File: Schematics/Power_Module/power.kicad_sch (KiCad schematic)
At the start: 67 parts, among them J2 ScrewSwitch, J3 Battery, J6 ScrewSwitch, J7 Battery, Q1 AO4447A, Q2 AO4447A, U1 LMR51430YDDCR, U10 TPS61175PWPR, U2 LMR51430YDDCR, U3 ACS37041KLHBLT-010B3, U4 AMS1117-3.3, U5 ACS37041KLHBLT-010B3, U6 LM66100DCKR, U7 LM66100DCKR, U8 LM66100DCKR

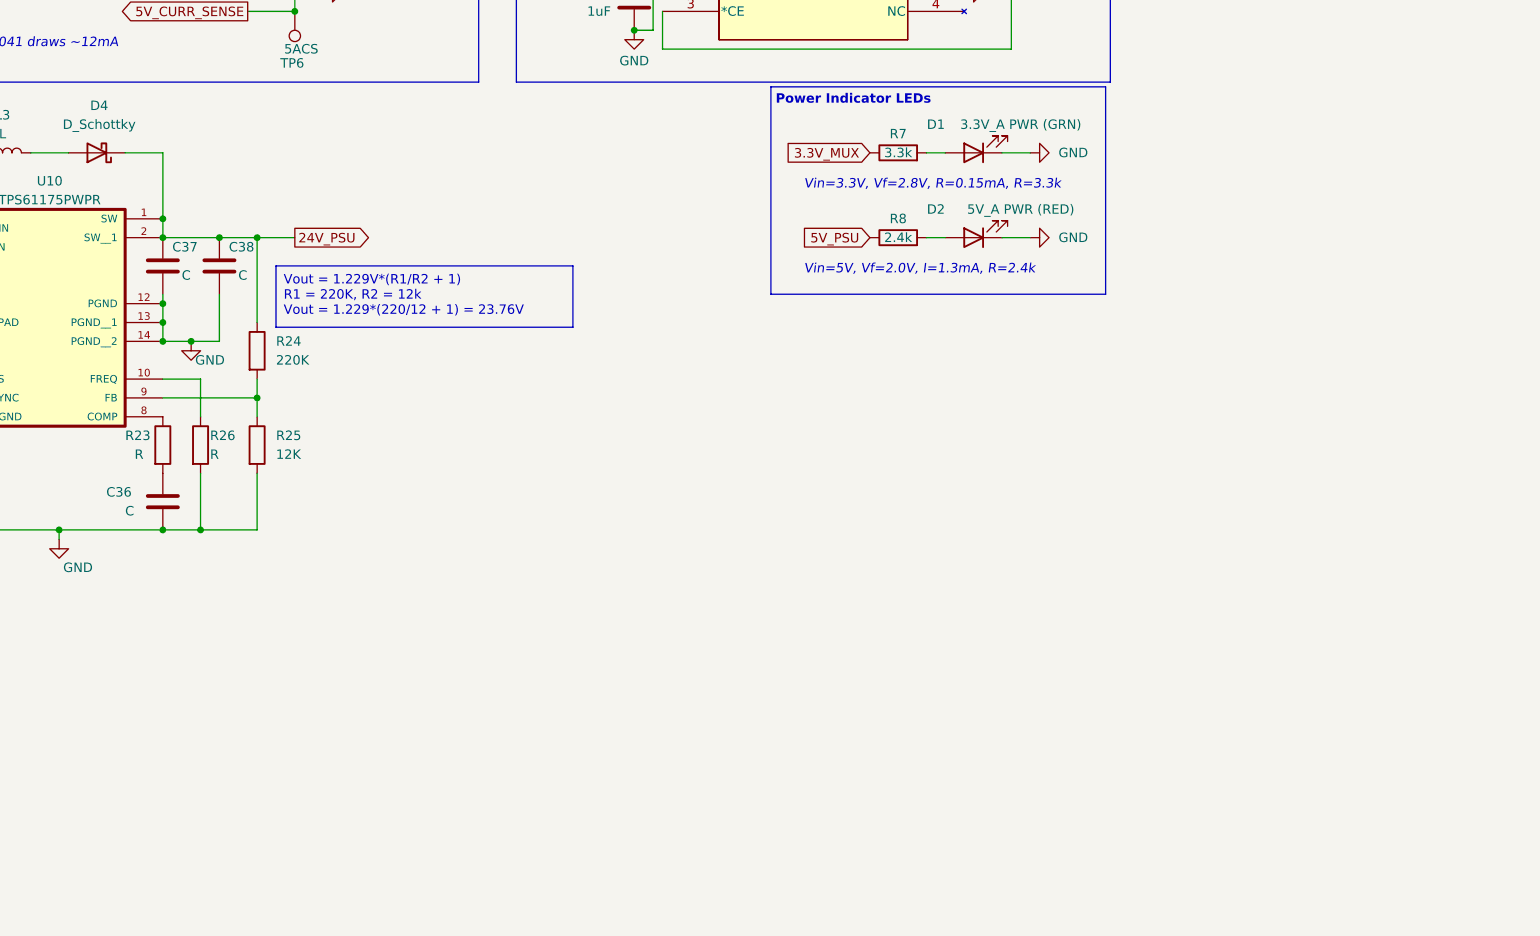
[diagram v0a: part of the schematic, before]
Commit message: cleaned up boost pdf & lcsc and noted next steps
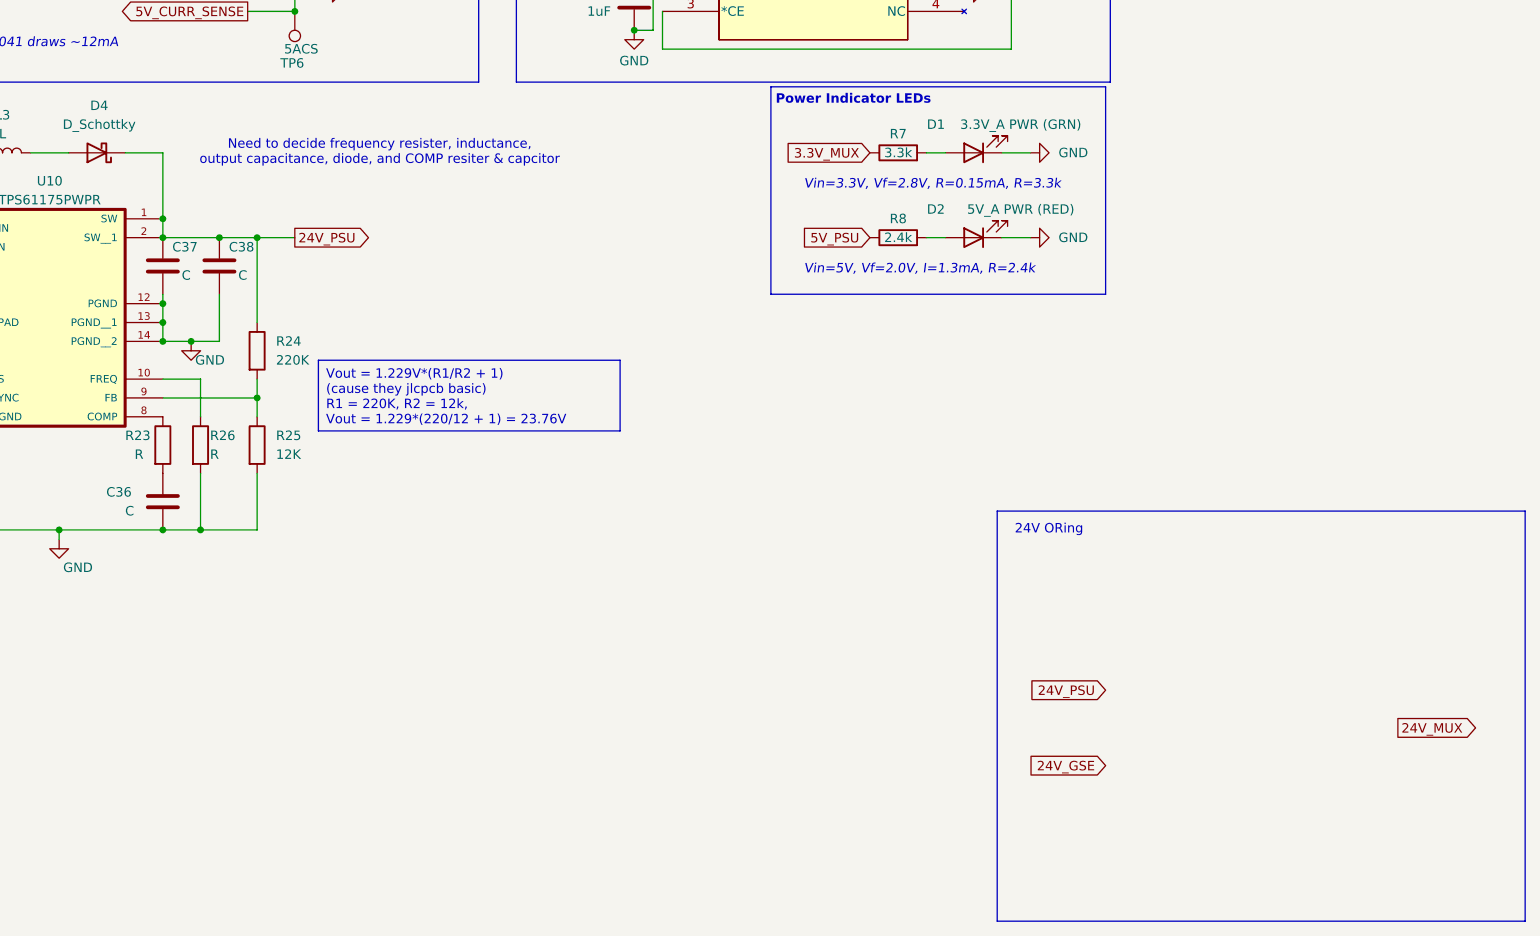
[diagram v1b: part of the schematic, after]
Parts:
- U10: LCSC (none) -> C43276
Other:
- note added: "24V ORing"
- note added: "Need to decide frequency resister, inductance, output capacitance, diode, and COMP resiter & capcitor"
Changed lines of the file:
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@@
+	)
+	(rectangle
+		(start 269.875 140.97)
+		(end 340.995 196.215)
+		(stroke
+			(width 0)
+			(type default)
+		)
+		(fill
+			(type none)
+		)
 	)
 	(rectangle
@@
 		)
 	)
-	(text_box "Vout = 1.229V*(R1/R2 + 1)\nR1 = 220K, R2 = 12k\nVout = 1.229*(220/12 + 1) = 23.76V"
-		(exclude_from_sim no)
-		(at 172.72 107.95 0)
-		(size 40.005 8.255)
+	(text_box "Vout = 1.229V*(R1/R2 + 1)\n(cause they jlcpcb basic)\nR1 = 220K, R2 = 12k, \nVout = 1.229*(220/12 + 1) = 23.76V"
+		(exclude_from_sim no)
+		(at 178.435 120.65 0)
+		(size 40.64 9.525)
 		(stroke
 			(width 0)
@@
 		)
 	)
+	(text "Need to decide frequency resister, inductance, \noutput capacitance, diode, and COMP resiter & capcitor"
+		(exclude_from_sim no)
+		(at 186.69 92.71 0)
+		(effects
+			(font
+				(size 1.27 1.27)
+			)
+		)
+	)
 	(text "3.3V USB Regulator"
 		(exclude_from_sim no)
@@
 			)
 			(justify left bottom)
+		)
+	)
+	(text "24V ORing"
+		(exclude_from_sim no)
+		(at 276.86 143.51 0)
+		(effects
+			(font
+				(size 1.27 1.27)
+			)
 		)
 	)
@@
 		)
 	)
+	(global_label "24V_MUX"
+		(shape output)
+		(at 323.85 170.18 0)
+		(fields_autoplaced yes)
+		(effects
+			(font
+				(size 1.27 1.27)
+			)
+			(justify left)
+		)
+		(property "Intersheetrefs" "${INTERSHEET_REFS}"
+			(at 335.3018 170.18 0)
+			(effects
+				(font
+					(size 1.27 1.27)
+				)
+				(justify left)
+				(hide yes)
+			)
+		)
+	)
 	(global_label "5V_PSU"
 		(shape output)
@@
 		)
 	)
+	(global_label "24V_PSU"
+		(shape input)
+		(at 284.48 165.1 180)
+		(fields_autoplaced yes)
+		(effects
+			(font
+				(size 1.27 1.27)
+			)
+			(justify right)
+		)
+		(property "Intersheetrefs" "${INTERSHEET_REFS}"
+			(at 273.2096 165.1 0)
+			(effects
+				(font
+					(size 1.27 1.27)
+				)
+				(justify right)
+				(hide yes)
+			)
+		)
+	)
 	(global_label "BATT"
 		(shape input)
@@
 		(property "Intersheetrefs" "${INTERSHEET_REFS}"
 			(at 99.401 102.87 0)
+			(effects
+				(font
+					(size 1.27 1.27)
+				)
+				(justify right)
+				(hide yes)
+			)
+		)
+	)
+	(global_label "24V_GSE"
+		(shape input)
+		(at 284.48 175.26 180)
+		(fields_autoplaced yes)
+		(effects
+			(font
+				(size 1.27 1.27)
+			)
+			(justify right)
+		)
+		(property "Intersheetrefs" "${INTERSHEET_REFS}"
+			(at 273.3911 175.26 0)
 			(effects
 				(font
@@
 			)
 		)
-		(property "Datasheet" ""
+		(property "Datasheet" "${KIPRJMOD}/../../Datasheets/tps61175.pdf"
 			(at 139.7 115.57 0)
 			(effects
@@
 			(at 139.7 115.57 0)
 			(effects
+				(font
+					(size 1.27 1.27)
+				)
+				(hide yes)
+			)
+		)
+		(property "LCSC" "C43276"
+			(at 139.7 115.57 0)
+			(effects

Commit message: adding power ORing circuit
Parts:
- added C39, C41, C42, C43: 1uF, Capacitor_SMD:C_0603_1608Metric, symbol Device:C
- added C40: 100uF, symbol Device:C_Polarized
- added Q3, Q4: AO3400A, Package_TO_SOT_SMD:SOT-23, symbol Transistor_FET:AO3400A
- added U14, U15: LM74700QDBVRQ1, Package_TO_SOT_SMD:SOT-23-6, symbol Power_Management:LM74700
- J7: value Battery -> GSE
- TP2: value GND1 -> BATT_GND1
- TP9: value GND1 -> GSE_GND1
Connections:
- net 24V_GSE: now also C39.1, C42.1, Q3.2 (S), U14.1 (VCAP), U14.3 (EN), U14.6 (ANODE)
- net 24V_MUX: now also C40.1, Q3.3 (D), Q4.3 (D), U14.4 (CATHODE), U15.4 (CATHODE)
- net 24V_PSU: now also C41.2, C43.2, Q4.2 (S), U15.1 (VCAP), U15.3 (EN), U15.6 (ANODE)
- net GND: now also C39.2, C40.2, C41.1, C42.2, C43.1, U14.2 (GND), U15.2 (GND)
- net BATT renamed V_BATT
- new net: Q4.1 (G), U15.5 (GATE)
- new net: Q3.1 (G), U14.5 (GATE)
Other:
- note added: "Battery side needs GND protection circuitry"
- note added: "Primary 24V Boost Regulator"
- moved on the sheet: C33, C34, C35, C36, C37, C38, D1, D2, D4, J2, J3, J6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

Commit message: add equations for Boost and instructions for buck design changes
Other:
- note added: "Switch 2 500000 Hz system!! (less switching loss) originally designed for component footprint Now design for increase efficient!!"
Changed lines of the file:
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@@
+		)
+	)
+	(text_box "Equations:\nD = 1 - Vin/Vo\nT = 1/F\nIin = Vin/(R(1-D)^2)\ndetla_IL = 30% of IL\nL = VinDT/L\nLcrit = RT/2(1-D)^2D (when IL = 0)\nIL_max = Iin + 1/2(delta_IL)\ndelta_Vc = VoDT/RC\nID_avg = Iin(1-D)\nId_max = IL_max\nVc_max = Vo\nIc_rms = sqrt(DIin^2 + (1-D)(Iin - Io) \n\n\nConstants:\nF = 200KHz to 2.2MHz (Choose lowest frequency feasable, smaller F -> large L and C)\nVin_max = 12.6V\nVin_nominal = 11.1V\nVin_min = 7.5V\nVo = 23.76V ~ 24V\nPo_max = 10W\nPo_min = 1W\nD_max = 1 - 7.5/24\nD_min = 1 - 12.6/24\n\n\n\n"
+		(exclude_from_sim no)
+		(at 251.8918 169.164 0)
+		(size 58.166 61.7982)
+		(stroke
+			(width 0)
+			(type default)
+		)
+		(fill
+			(type none)
+		)
+		(effects
+			(font
+				(size 1.27 1.27)
+			)
+			(justify left top)
 		)
 	)
@@
 		)
 	)
+	(text "Switch 2 500000 Hz system!! (less switching loss)\noriginally designed for component footprint\nNow design for increase efficient!!"
+		(exclude_from_sim no)
+		(at -48.26 2.54 0)
+		(effects
+			(font
+				(size 1.27 1.27)
+				(thickness 0.254)
+				(bold yes)
+			)
+		)
+	)

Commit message: Update power.kicad_sch
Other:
- note added: "Switched to a 500 000 Hz system for increase in efficiency."
- note removed: "Switch 2 500000 Hz system!! (less switching loss) originally designed for component footprint Now design for increase efficient!!"
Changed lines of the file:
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@@
 		)
 	)
-	(text_box "Constants:\nT = 1/1100000\nVin = 24V\nVout = 5\nD = 5/24\n\nP = 0.2W\nLcrit = 0.5(1-.2083)(5^2/0.2)*(1/1100000) = 45uH\n\nP=1W (typical with RF transmition)\nLcrit = 0.5(1-.2083)(5^2/1)*(1/1100000) = 9uH\ndelta IL = 0.3(1/5) = 0.06A\nL = 5(1-0.2083)(1/1100000)/(0.08) = 60uH\nILmax = (1/5) + 0.5*(0.06) = 0.23A\n\nChose Inductor 68uH, ILmax = 1A\ndelta_IL = 5(1-0.2083)/(1100000*68*10^-6) = 0.053A\ndelta_Vo = 2%*5 = 0.1V\nC = 0.053/(8*1100000*0.1) = 0.06uF"
+	(text_box "Constants:\nT = 1/500000\nVin = 24V\nVout = 5\nD = 5/24\n\nP = 0.2W\nLcrit = 0.5(1-0.2083)(5^2/0.2)*(1/500000) = 99uH\n\nP=1W (typical with RF transmition)\nLcrit = 0.5(1-0.2083)(5^2/1)*(1/500000) = 20uH\n\ndelta IL = 0.3(1/5) = 0.06A\nL = 5(1-0.2083)(1/500000)/(0.06) = 132uH\nILmax = (1/5) + 0.5*(0.06) = 0.23A\n\nChose Inductor 130uH, ILmax = 1A\ndelta_IL = 5(1-0.2083)/(500000*130*10^-6) = 0.061A\ndelta_Vo = 2%*5 = 0.1V\nC = 0.061/(8*500000*0.1) = 0.15uF"
 		(exclude_from_sim no)
 		(at -80.645 93.345 0)
@@
 		)
 	)
-	(text_box "Constants:\nT = 1/1100000\nVin = 24V\nVout = 3.3V\nD = 3.3/24 = 0.1375\n\nP = 0.5W (estimate with one module powered)\nLcrit = 0.5*(1-0.1375)*(3.3^2/0.5)*(1/1100000) = 2.6uH\n\nPo = 3W (estimate of all 3.3V modules)\nLcrit = 0.5*(1-0.1375)*(3.3^2/3)*(1/1100000) = 0.43uH\n\ndelta_IL = 0.3*(3/3.3) = 0.273A\nL = 3.3*(1-0.1375)/(1100000*0.273) = 9.5uH\nILmax = (3/3.3) + 0.5*0.273 = 1.05A\n\n\nChose 10uH Inductor, ILmax = 2.5\ndelta_IL = 3.3*(1-0.1375)/(1100000*10*10^-6) = 0.26A\ndelta_Vo = 2%*3.3 = 0.066V\nC = 0.26/(8*1100000*0.066) = 0.45uF"
-		(exclude_from_sim no)
-		(at -80.645 46.99 0)
-		(size 60.325 44.45)
+	(text_box "Constants:\nT = 1/500000\nVin = 24V\nVout = 3.3V\nD = 3.3/24 = 0.1375\n\nP = 0.5W (estimate with one module powered)\nLcrit = 0.5*(1-0.1375)*(3.3^2/0.5)*(1/500000) = 18.79uH\n\nPo = 3W (estimate of all 3.3V modules)\nLcrit = 0.5*(1-0.1375)*(3.3^2/3)*(1/500000) = 3.13uH\n\ndelta_IL = 0.3*(3/3.3) = 0.273A\nL = 3.3*(1-0.1375)/(500000*0.273) = 20.85uH\nILmax = (3/3.3) + 0.5*0.273 = 1.05A\n\n\nChose 22uH Inductor, ILmax = 2.2 \ndelta_IL = 3.3*(1-0.1375)/(500000*22*10^-6) = 0.26A\ndelta_Vo = 2%*3.3 = 0.066V\nC = 0.26/(8*500000*0.066) = 0.98uF"
+		(exclude_from_sim no)
+		(at -81.28 46.99 0)
+		(size 62.23 44.45)
 		(stroke
 			(width 0)
@@
 		)
 	)
-	(text "Switch 2 500000 Hz system!! (less switching loss)\noriginally designed for component footprint\nNow design for increase efficient!!"
+	(text "Switched to a 500 000 Hz system for increase in efficiency."
 		(exclude_from_sim no)
 		(at -48.26 2.54 0)

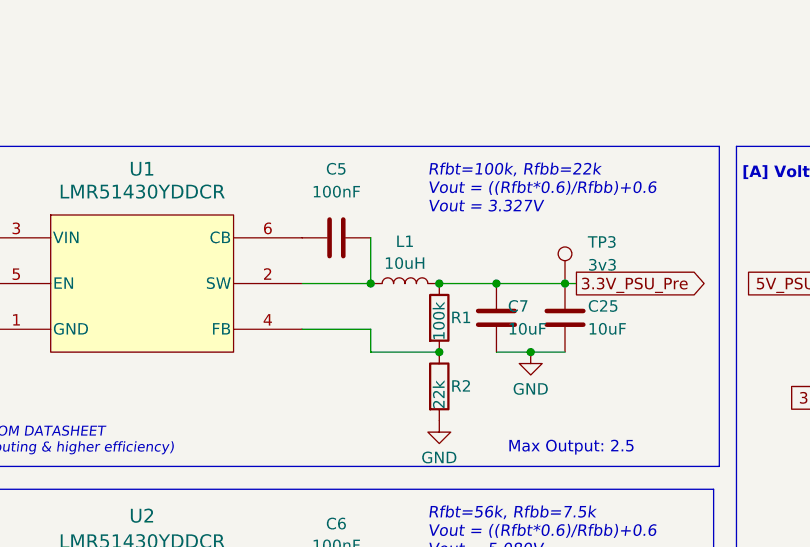
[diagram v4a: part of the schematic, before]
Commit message: Update power.kicad_sch
Changed frequency to 500 000Hz and updated schematics (not the new footprint)
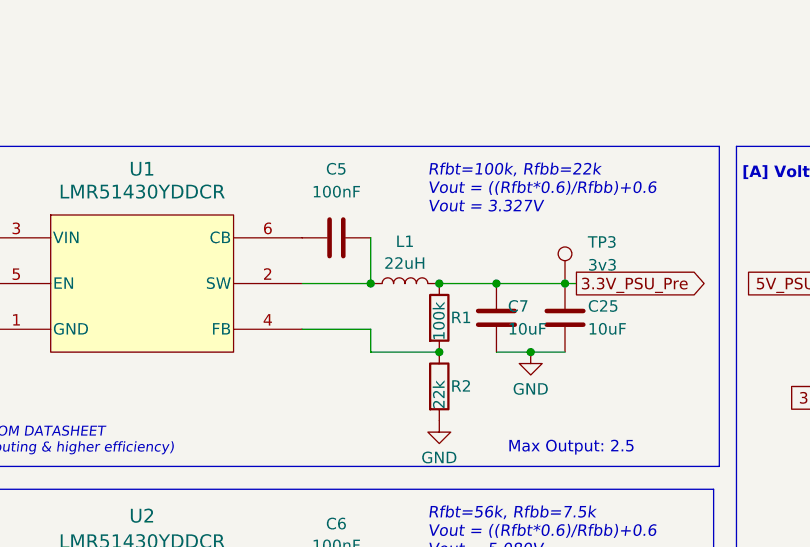
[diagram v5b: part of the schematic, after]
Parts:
- L1: value 10uH -> 22uH; Digikey 445-181622-1-ND -> 587-2002-2-ND
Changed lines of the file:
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@@
 			)
 		)
-		(property "Value" "10uH"
+		(property "Value" "22uH"
 			(at 88.9 28.2546 90)
 			(effects
@@
 			)
 		)
-		(property "Datasheet" "${KIPRJMOD}/../../Datasheets/inductor_vls5045ex-h"
+		(property "Datasheet" "https://mm.digikey.com/Volume0/opasdata/d220001/medias/docus/610/NR8040T220M_SS.pdf"
 			(at 88.9 30.48 0)
 			(effects
@@
 			)
 		)
-		(property "Digikey" "445-181622-1-ND"
+		(property "Digikey" "587-2002-2-ND"
 			(at 88.9 30.48 90)
 			(effects

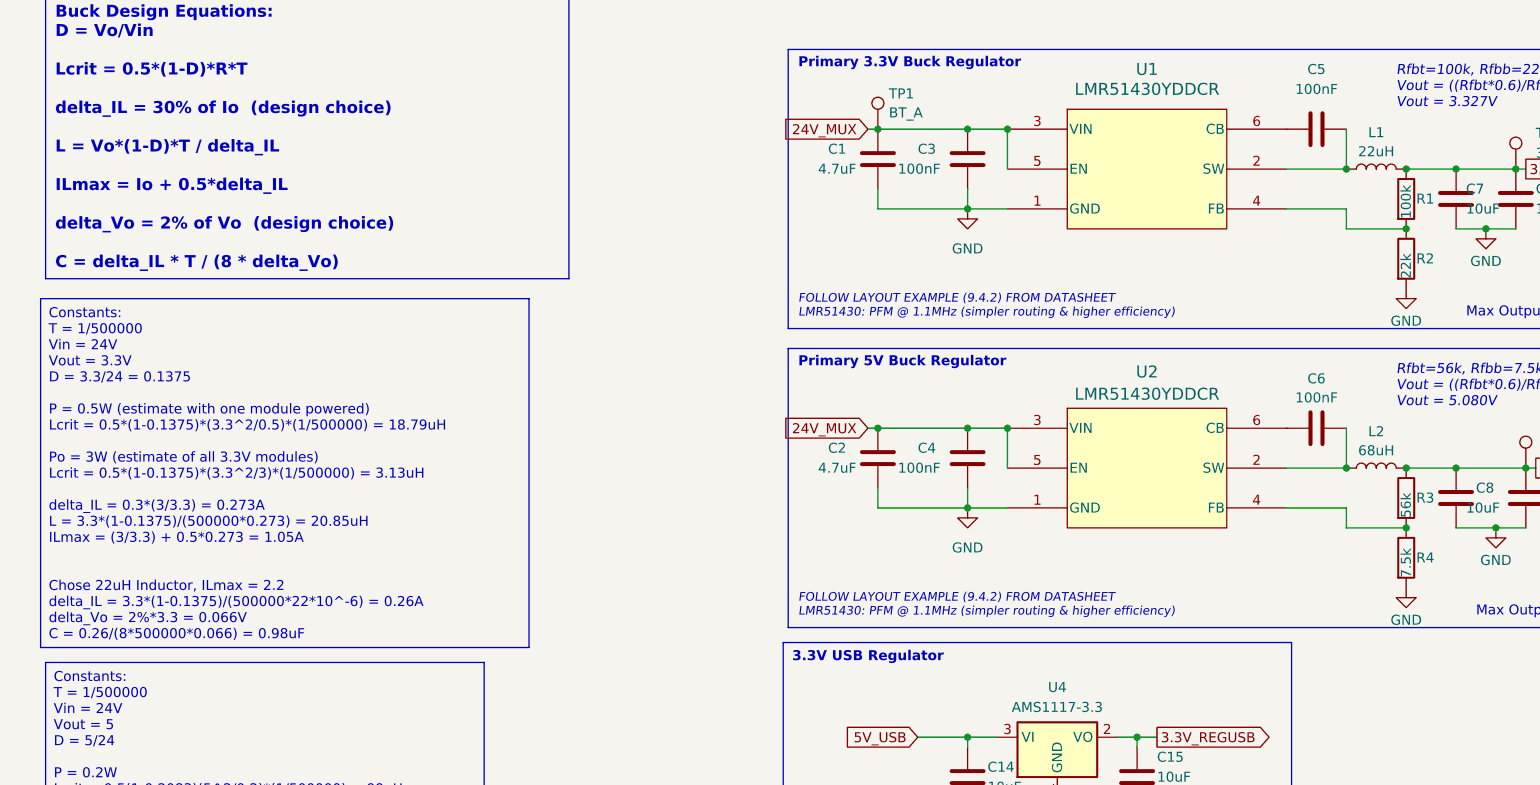
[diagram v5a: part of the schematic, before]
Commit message: 3.3V inductor changed to 27uF 3.6A
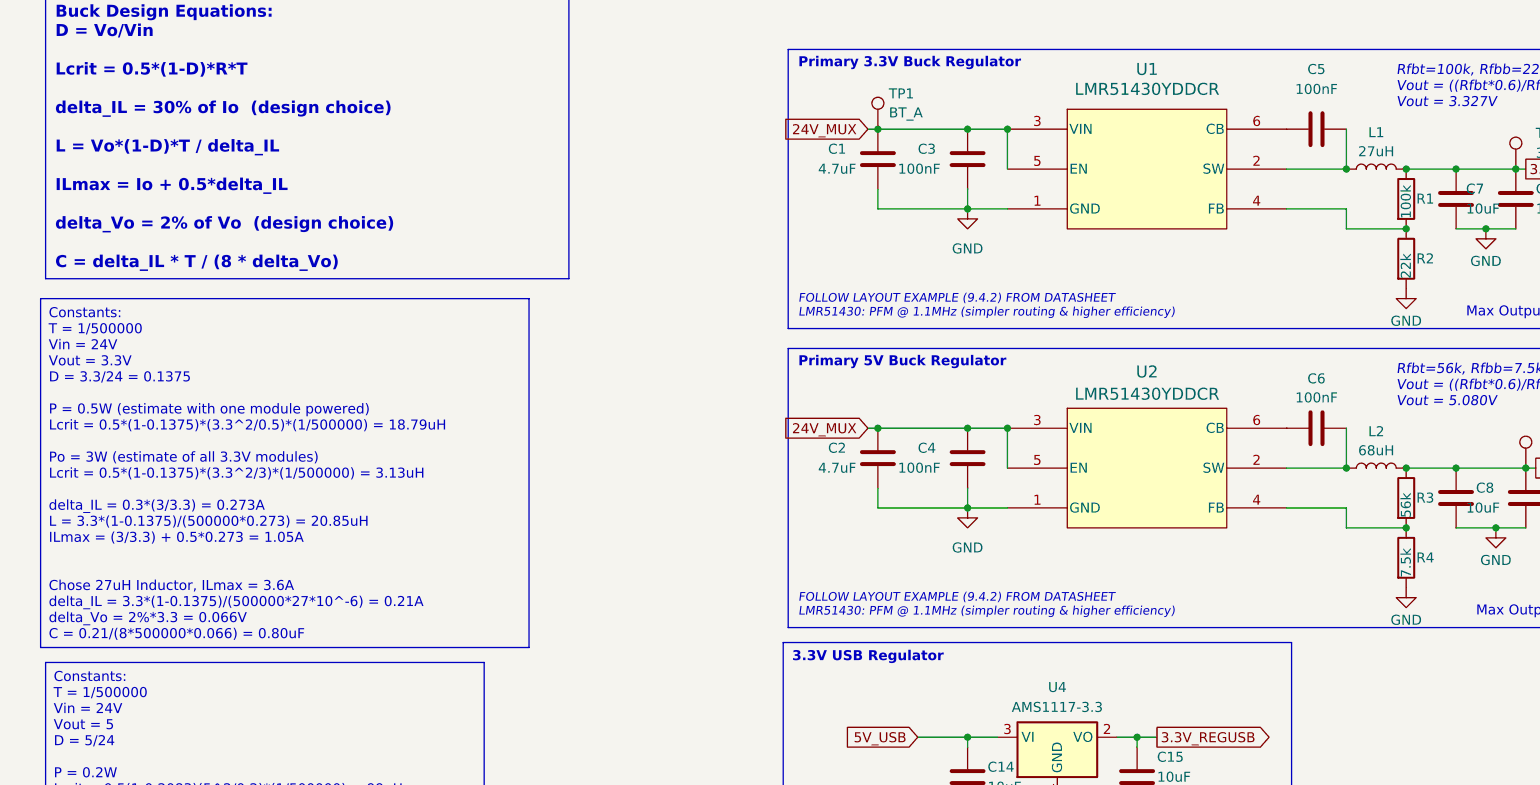
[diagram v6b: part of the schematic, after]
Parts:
- L1: value 22uH -> 27uH; Digikey 587-2002-2-ND -> 118-SRR1260A-270MTR-ND
